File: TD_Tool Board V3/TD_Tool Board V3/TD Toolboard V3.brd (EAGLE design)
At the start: 54.2 x 49 mm, 139 parts, among them J3 JST-MICROFIT, M1 NMOSFET_WSD3066DN33, M2 CJ3400, M3 CJ3400, M4 CJ3400, P1 TPS54202_BUCKCONV, P2 3.3V, U1 RP2040, U2 W25Q128, U3 SN65HVD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

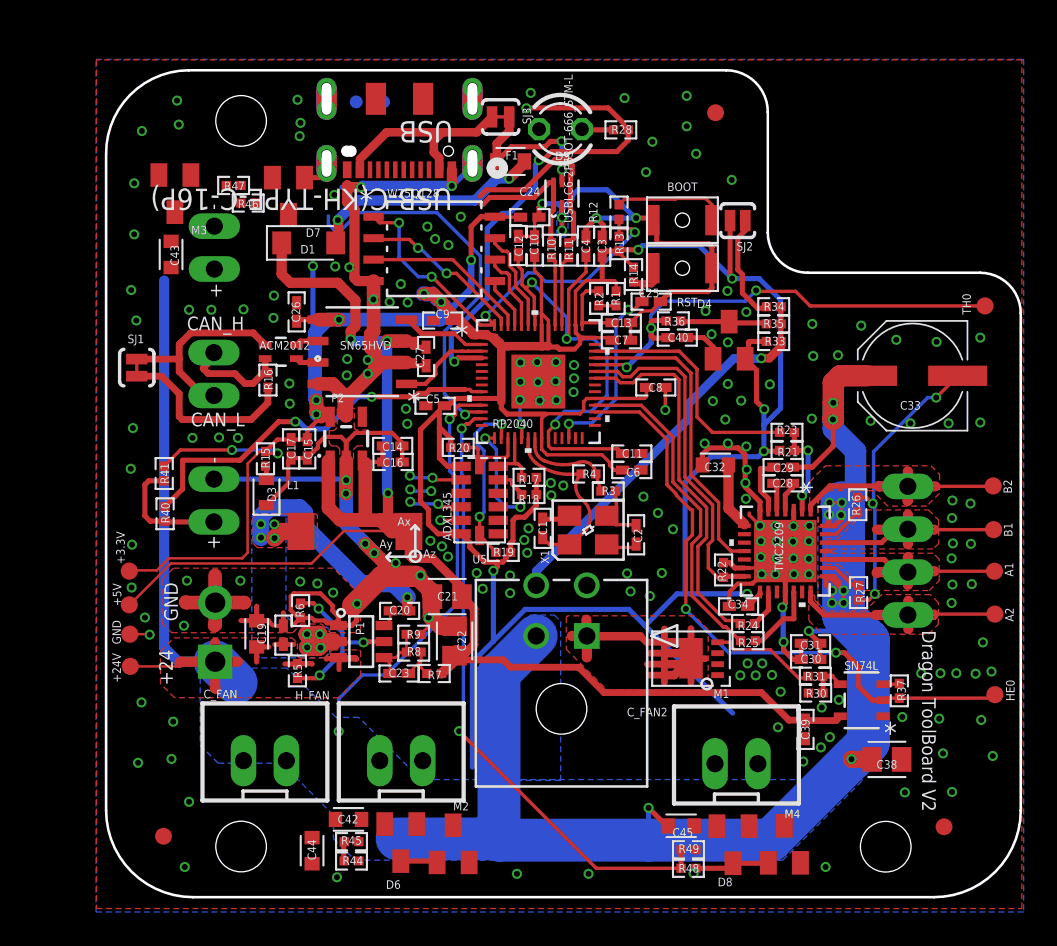
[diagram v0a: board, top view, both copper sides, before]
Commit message: Made the required changes - renamed toolboard to V3
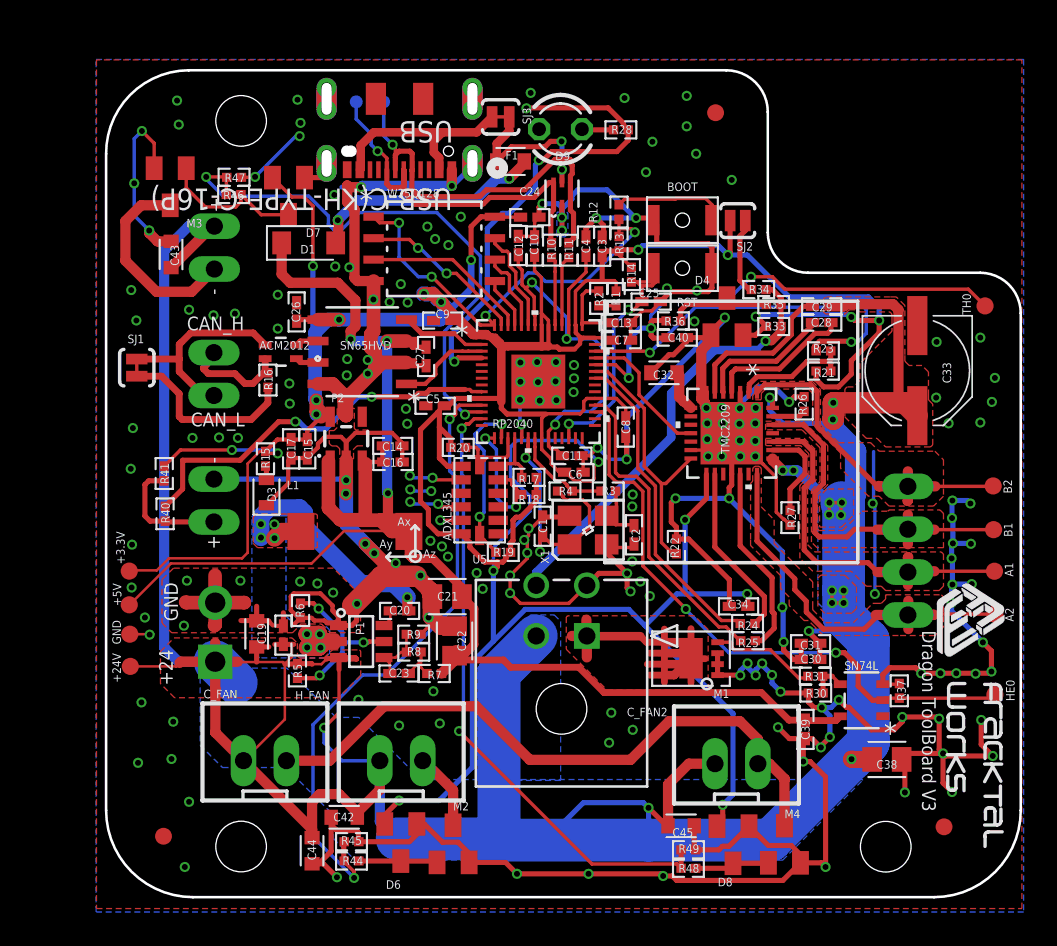
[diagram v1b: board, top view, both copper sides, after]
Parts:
- added U$1: (no value), FracktalWorks_Eagle_Library:FWLOGO_SMALL
- moved C28 9.80 mm to (47.9, 39.0)
- moved C29 9.80 mm to (47.9, 40.0)
- moved U7 7.67 mm to (42.6, 32.4)
- moved R26 6.76 mm to (46.9, 34.2)
- moved C32 6.25 mm to (38.6, 36.0)
- moved R27 6.02 mm to (46.0, 27.4)
- moved R23 5.29 mm to (48.0, 37.3)
- moved R21 5.17 mm to (48.0, 36.1)
- moved C11 3.56 mm to (33.1, 31.1)
- moved C6 3.43 mm to (33.2, 30.1)
- moved R22 3.12 mm to (39.3, 25.7)
- moved C8 2.95 mm to (36.3, 32.8), turned to 270 degrees
- moved R4 1.73 mm to (32.7, 29.0)
- moved D4 1.40 mm to (42.3, 39.3)
- moved R34 1.35 mm to (44.2, 40.9)
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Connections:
- removed net N$2: M_FAN.1
- net +24V: now also M_FAN.1
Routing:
- net GND: track 201.2 -> 394.4 mm, vias 207 -> 198
- net +24V: track 138.1 -> 228.4 mm, vias 13 -> 17
- net N$4: track 0.00 -> 38.2 mm
- net +3.3V: track 235.7 -> 269.6 mm, vias 15 -> 20
- net USB1_P: track 8.50 -> 22.5 mm, vias 0 -> 1
- net USB1_N: track 11.5 -> 23.5 mm, vias 0 -> 1
- net N$3: track 0.00 -> 12.0 mm
- net FAN0: track 26.0 -> 37.6 mm
- net FAN1: track 23.0 -> 33.5 mm, vias 1 -> 2
- net E0_DIAG: track 18.4 -> 8.31 mm
- net A2: track 13.6 -> 23.2 mm
- net B1: track 13.9 -> 23.4 mm
- net A1: track 13.9 -> 22.8 mm
- net FAN1G: track 0.00 -> 8.75 mm
- net STEP: track 2.20 -> 10.3 mm
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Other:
- board text added: "Dragon ToolBoard V3"
- board text removed: "Dragon ToolBoard V2"
